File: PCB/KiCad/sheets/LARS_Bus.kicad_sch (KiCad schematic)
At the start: 24 parts, among them J28 USB1, J29 USB2, U10 USBLC6-2SC6, U11 TCAN1057AVDRQ1, U12 USBLC6-2SC6

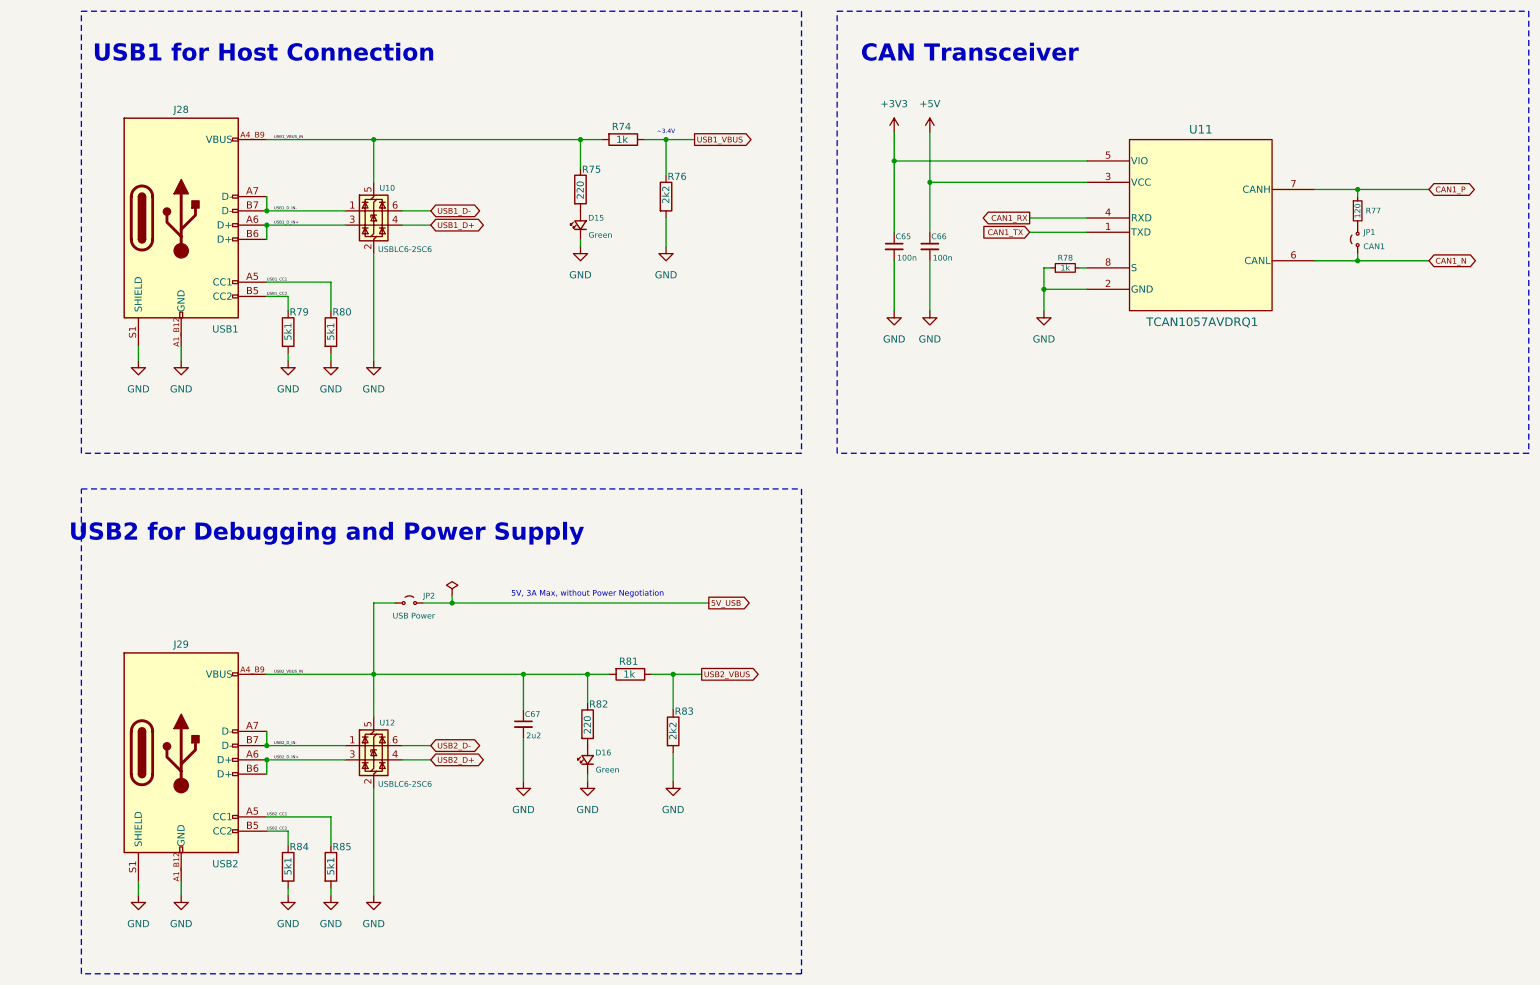
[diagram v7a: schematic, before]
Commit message: PCB: add XOR gate for RC Receiver
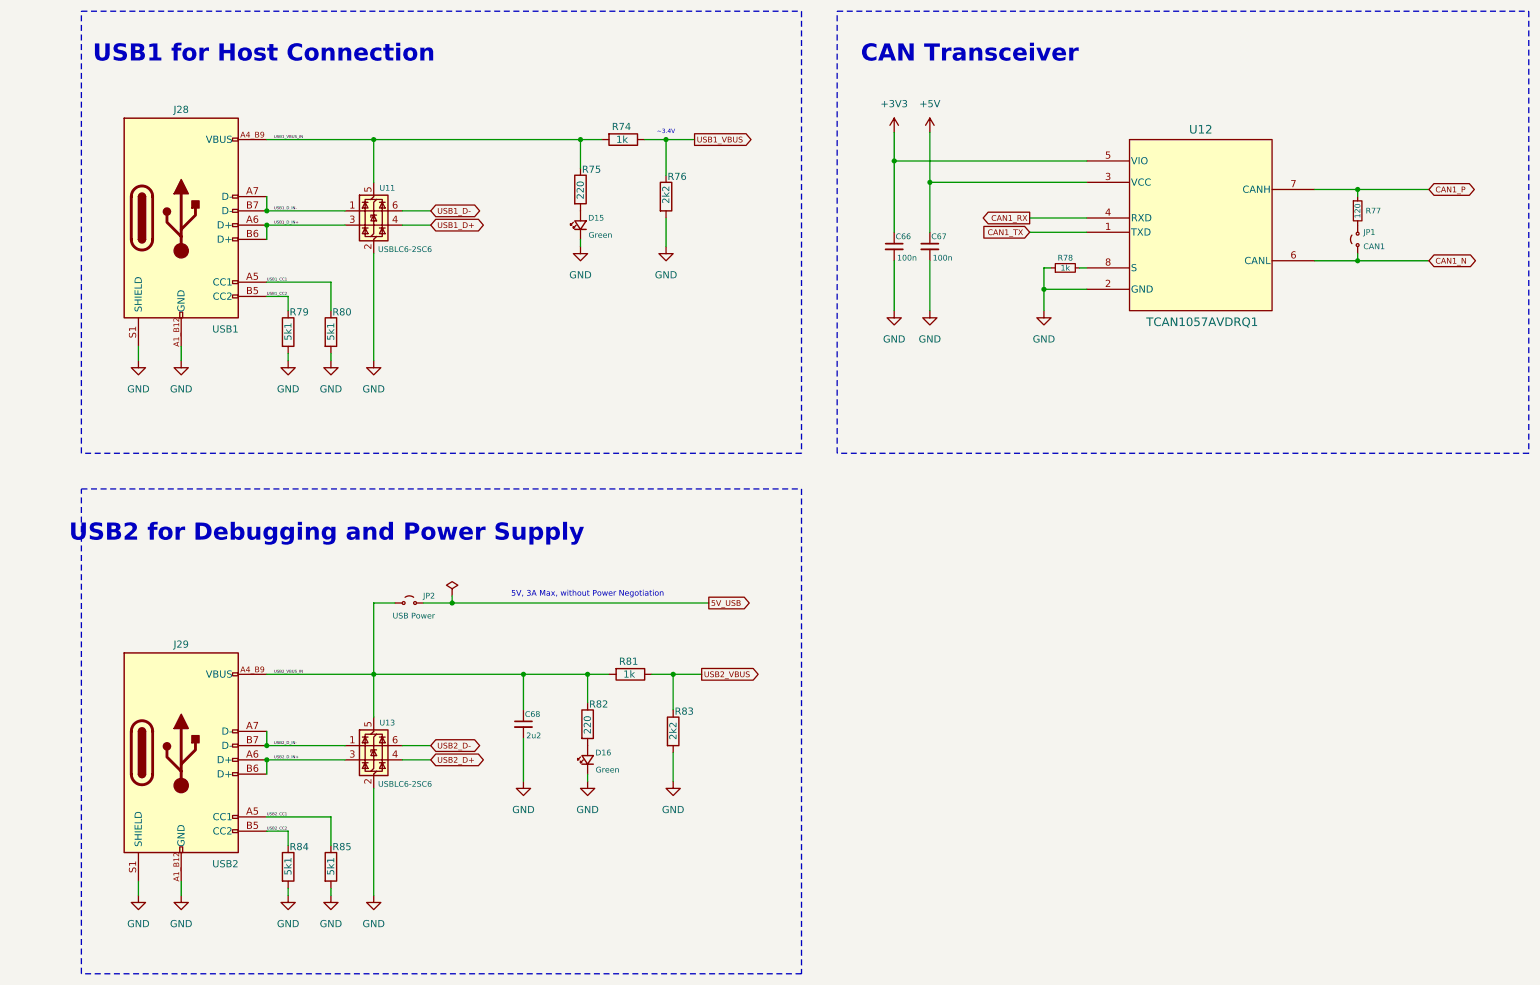
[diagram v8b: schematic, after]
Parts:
- renumbered C65 to C66, C66 to C67, C67 to C68, U10 to U11, U11 to U12, U12 to U13
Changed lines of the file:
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@@
 		(dnp no)
 		(fields_autoplaced yes)
-		(property "Reference" "#PWR0175"
+		(property "Reference" "#PWR0177"
 			(at 123.19 67.31 0)
 			(effects
@@
 			(project "hardware_interface"
 				(path "/ffedf44c-a51a-4124-b6d3-e3f1f256e9ac/31b4cc6e-8490-43f3-a459-a8f45a93fb3e"
-					(reference "#PWR0175")
+					(reference "#PWR0177")
 					(unit 1)
 				)
@@
 		(dnp no)
 		(fields_autoplaced yes)
-		(property "Reference" "#PWR0177"
+		(property "Reference" "#PWR0179"
 			(at 170.18 78.74 0)
 			(effects
@@
 			(project "hardware_interface"
 				(path "/ffedf44c-a51a-4124-b6d3-e3f1f256e9ac/31b4cc6e-8490-43f3-a459-a8f45a93fb3e"
-					(reference "#PWR0177")
+					(reference "#PWR0179")
 					(unit 1)
 				)
@@
 		(dnp no)
 		(fields_autoplaced yes)
-		(property "Reference" "#PWR0182"
+		(property "Reference" "#PWR0184"
 			(at 63.5 87.63 0)
 			(effects
@@
 			(project "hardware_interface"
 				(path "/ffedf44c-a51a-4124-b6d3-e3f1f256e9ac/31b4cc6e-8490-43f3-a459-a8f45a93fb3e"
-					(reference "#PWR0182")
+					(reference "#PWR0184")
 					(unit 1)
 				)
@@
 		(dnp no)
 		(fields_autoplaced yes)
-		(property "Reference" "#PWR0172"
+		(property "Reference" "#PWR0174"
 			(at 163.83 44.45 0)
 			(effects
@@
 			(project "hardware_interface"
 				(path "/ffedf44c-a51a-4124-b6d3-e3f1f256e9ac/31b4cc6e-8490-43f3-a459-a8f45a93fb3e"
-					(reference "#PWR0172")
+					(reference "#PWR0174")
 					(unit 1)
 				)
@@
 		(on_board yes)
 		(dnp no)
-		(property "Reference" "U12"
+		(property "Reference" "U13"
 			(at 72.136 145.796 0)
 			(effects
@@
 			(project "hardware_interface"
 				(path "/ffedf44c-a51a-4124-b6d3-e3f1f256e9ac/31b4cc6e-8490-43f3-a459-a8f45a93fb3e"
-					(reference "U12")
+					(reference "U13")
 					(unit 1)
 				)
@@
 		(dnp no)
 		(fields_autoplaced yes)
-		(property "Reference" "#PWR0176"
+		(property "Reference" "#PWR0178"
 			(at 163.83 78.74 0)
 			(effects
@@
 			(project "hardware_interface"
 				(path "/ffedf44c-a51a-4124-b6d3-e3f1f256e9ac/31b4cc6e-8490-43f3-a459-a8f45a93fb3e"
-					(reference "#PWR0176")
+					(reference "#PWR0178")
 					(unit 1)
 				)
@@
 		(on_board yes)
 		(dnp no)
-		(property "Reference" "C66"
+		(property "Reference" "C67"
 			(at 170.434 59.182 0)
 			(effects
@@
 			(project "hardware_interface"
 				(path "/ffedf44c-a51a-4124-b6d3-e3f1f256e9ac/31b4cc6e-8490-43f3-a459-a8f45a93fb3e"
-					(reference "C66")
+					(reference "C67")
 					(unit 1)
 				)
@@
 		(dnp no)
 		(fields_autoplaced yes)
-		(property "Reference" "#PWR0185"
+		(property "Reference" "#PWR0187"
 			(at 109.22 162.56 0)
 			(effects
@@
 			(project "hardware_interface"
 				(path "/ffedf44c-a51a-4124-b6d3-e3f1f256e9ac/31b4cc6e-8490-43f3-a459-a8f45a93fb3e"
-					(reference "#PWR0185")
+					(reference "#PWR0187")
 					(unit 1)
 				)
@@
 		(dnp no)
 		(fields_autoplaced yes)
-		(property "Reference" "#PWR0189"
+		(property "Reference" "#PWR0191"
 			(at 55.88 182.88 0)
 			(effects
@@
 			(project "hardware_interface"
 				(path "/ffedf44c-a51a-4124-b6d3-e3f1f256e9ac/31b4cc6e-8490-43f3-a459-a8f45a93fb3e"
-					(reference "#PWR0189")
+					(reference "#PWR0191")
 					(unit 1)
 				)
@@
 		(dnp no)
 		(fields_autoplaced yes)
-		(property "Reference" "#PWR0178"
+		(property "Reference" "#PWR0180"
 			(at 190.5 78.74 0)
 			(effects
@@
 			(project "hardware_interface"
 				(path "/ffedf44c-a51a-4124-b6d3-e3f1f256e9ac/31b4cc6e-8490-43f3-a459-a8f45a93fb3e"
-					(reference "#PWR0178")
+					(reference "#PWR0180")
 					(unit 1)
 				)
@@
 		(dnp no)
 		(fields_autoplaced yes)
-		(property "Reference" "#PWR0186"
+		(property "Reference" "#PWR0188"
 			(at 124.46 162.56 0)
 			(effects
@@
 			(project "hardware_interface"
 				(path "/ffedf44c-a51a-4124-b6d3-e3f1f256e9ac/31b4cc6e-8490-43f3-a459-a8f45a93fb3e"
-					(reference "#PWR0186")
+					(reference "#PWR0188")
 					(unit 1)
 				)
@@
 		(dnp no)
 		(fields_autoplaced yes)
-		(property "Reference" "#PWR0179"
+		(property "Reference" "#PWR0181"
 			(at 29.21 87.63 0)
 			(effects
@@
 			(project "hardware_interface"
 				(path "/ffedf44c-a51a-4124-b6d3-e3f1f256e9ac/31b4cc6e-8490-43f3-a459-a8f45a93fb3e"
-					(reference "#PWR0179")
+					(reference "#PWR0181")
 					(unit 1)
 				)
@@
 		(dnp no)
 		(fields_autoplaced yes)
-		(property "Reference" "#PWR0191"
+		(property "Reference" "#PWR0193"
 			(at 71.12 182.88 0)
 			(effects
@@
 			(project "hardware_interface"
 				(path "/ffedf44c-a51a-4124-b6d3-e3f1f256e9ac/31b4cc6e-8490-43f3-a459-a8f45a93fb3e"
-					(reference "#PWR0191")
+					(reference "#PWR0193")
 					(unit 1)
 				)
@@
 		(dnp no)
 		(fields_autoplaced yes)
-		(property "Reference" "#PWR0180"
+		(property "Reference" "#PWR0182"
 			(at 36.83 87.63 0)
 			(effects
@@
 			(project "hardware_interface"
 				(path "/ffedf44c-a51a-4124-b6d3-e3f1f256e9ac/31b4cc6e-8490-43f3-a459-a8f45a93fb3e"
-					(reference "#PWR0180")
+					(reference "#PWR0182")
 					(unit 1)
 				)
@@
 		(dnp no)
 		(fields_autoplaced yes)
-		(property "Reference" "#PWR0183"
+		(property "Reference" "#PWR0185"
 			(at 71.12 87.63 0)
 			(effects
@@
 			(project "hardware_interface"
 				(path "/ffedf44c-a51a-4124-b6d3-e3f1f256e9ac/31b4cc6e-8490-43f3-a459-a8f45a93fb3e"
-					(reference "#PWR0183")
+					(reference "#PWR0185")
 					(unit 1)
 				)
@@
 		(dnp no)
 		(fields_autoplaced yes)
-		(property "Reference" "#PWR0181"
+		(property "Reference" "#PWR0183"
 			(at 55.88 87.63 0)
 			(effects
@@
 			(project "hardware_interface"
 				(path "/ffedf44c-a51a-4124-b6d3-e3f1f256e9ac/31b4cc6e-8490-43f3-a459-a8f45a93fb3e"
-					(reference "#PWR0181")
+					(reference "#PWR0183")
 					(unit 1)
 				)
@@
 		(dnp no)
 		(fields_autoplaced yes)
-		(property "Reference" "#PWR0174"
+		(property "Reference" "#PWR0176"
 			(at 107.95 67.31 0)
 			(effects
@@
 			(project "hardware_interface"
 				(path "/ffedf44c-a51a-4124-b6d3-e3f1f256e9ac/31b4cc6e-8490-43f3-a459-a8f45a93fb3e"
-					(reference "#PWR0174")
+					(reference "#PWR0176")
 					(unit 1)
 				)
@@
 		(dnp no)
 		(fields_autoplaced yes)
-		(property "Reference" "#PWR0173"
+		(property "Reference" "#PWR0175"
 			(at 170.18 44.45 0)
 			(effects
@@
 			(project "hardware_interface"
 				(path "/ffedf44c-a51a-4124-b6d3-e3f1f256e9ac/31b4cc6e-8490-43f3-a459-a8f45a93fb3e"
-					(reference "#PWR0173")
+					(reference "#PWR0175")
 					(unit 1)
 				)
@@
 		(on_board yes)
 		(dnp no)
-		(property "Reference" "C67"
+		(property "Reference" "C68"
 			(at 98.044 144.272 0)
 			(effects
@@
 			(project "hardware_interface"
 				(path "/ffedf44c-a51a-4124-b6d3-e3f1f256e9ac/31b4cc6e-8490-43f3-a459-a8f45a93fb3e"
-					(reference "C67")
+					(reference "C68")
 					(unit 1)
 				)
@@
 		(dnp no)
 		(fields_autoplaced yes)
-		(property "Reference" "#PWR0188"
+		(property "Reference" "#PWR0190"
 			(at 36.83 182.88 0)
 			(effects
@@
 			(project "hardware_interface"
 				(path "/ffedf44c-a51a-4124-b6d3-e3f1f256e9ac/31b4cc6e-8490-43f3-a459-a8f45a93fb3e"
-					(reference "#PWR0188")
+					(reference "#PWR0190")
 					(unit 1)
 				)
@@
 		(on_board yes)
 		(dnp no)
-		(property "Reference" "U11"
+		(property "Reference" "U12"
 			(at 218.44 40.132 0)
 			(effects
@@
 			(project "hardware_interface"
 				(path "/ffedf44c-a51a-4124-b6d3-e3f1f256e9ac/31b4cc6e-8490-43f3-a459-a8f45a93fb3e"
-					(reference "U11")
+					(reference "U12")
 					(unit 1)
 				)
@@
 		(on_board yes)
 		(dnp no)
-		(property "Reference" "U10"
+		(property "Reference" "U11"
 			(at 72.136 50.546 0)
 			(effects
@@
 			(project "hardware_interface"
 				(path "/ffedf44c-a51a-4124-b6d3-e3f1f256e9ac/31b4cc6e-8490-43f3-a459-a8f45a93fb3e"
-					(reference "U10")
+					(reference "U11")
 					(unit 1)
 				)
@@
 		(dnp no)
 		(fields_autoplaced yes)
-		(property "Reference" "#PWR0190"
+		(property "Reference" "#PWR0192"
 			(at 63.5 182.88 0)
 			(effects
@@
 			(project "hardware_interface"
 				(path "/ffedf44c-a51a-4124-b6d3-e3f1f256e9ac/31b4cc6e-8490-43f3-a459-a8f45a93fb3e"
-					(reference "#PWR0190")
+					(reference "#PWR0192")
 					(unit 1)
 				)
@@
 		(on_board yes)
 		(dnp no)
-		(property "Reference" "C65"
+		(property "Reference" "C66"
 			(at 164.084 59.182 0)
 			(effects
@@
 			(project "hardware_interface"
 				(path "/ffedf44c-a51a-4124-b6d3-e3f1f256e9ac/31b4cc6e-8490-43f3-a459-a8f45a93fb3e"
-					(reference "C65")
+					(reference "C66")
 					(unit 1)
 				)
@@
 		(dnp no)
 		(fields_autoplaced yes)
-		(property "Reference" "#PWR0184"
+		(property "Reference" "#PWR0186"
 			(at 97.79 162.56 0)
 			(effects
@@
 			(project "hardware_interface"
 				(path "/ffedf44c-a51a-4124-b6d3-e3f1f256e9ac/31b4cc6e-8490-43f3-a459-a8f45a93fb3e"
-					(reference "#PWR0184")
+					(reference "#PWR0186")
 					(unit 1)
 				)
@@
 		(dnp no)
 		(fields_autoplaced yes)
-		(property "Reference" "#PWR0187"
+		(property "Reference" "#PWR0189"
 			(at 29.21 182.88 0)
 			(effects
@@
 			(project "hardware_interface"
 				(path "/ffedf44c-a51a-4124-b6d3-e3f1f256e9ac/31b4cc6e-8490-43f3-a459-a8f45a93fb3e"
-					(reference "#PWR0187")
-					(unit 1)
-				)
+					(reference "#PWR0189")
+					(unit 1)
+				)
